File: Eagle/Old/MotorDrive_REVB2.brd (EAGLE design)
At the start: 127 x 58.4 mm, 74 parts, among them J8 J_MC32857, Q1 IRLB3036PBF, Q5 MC7812CTG, Q6 MC7805ACTG, Q7 Q_LTC490, U3 HIP4081A, U4 CD74ACT14, U5 ATMEGA328P, X1 HC49S

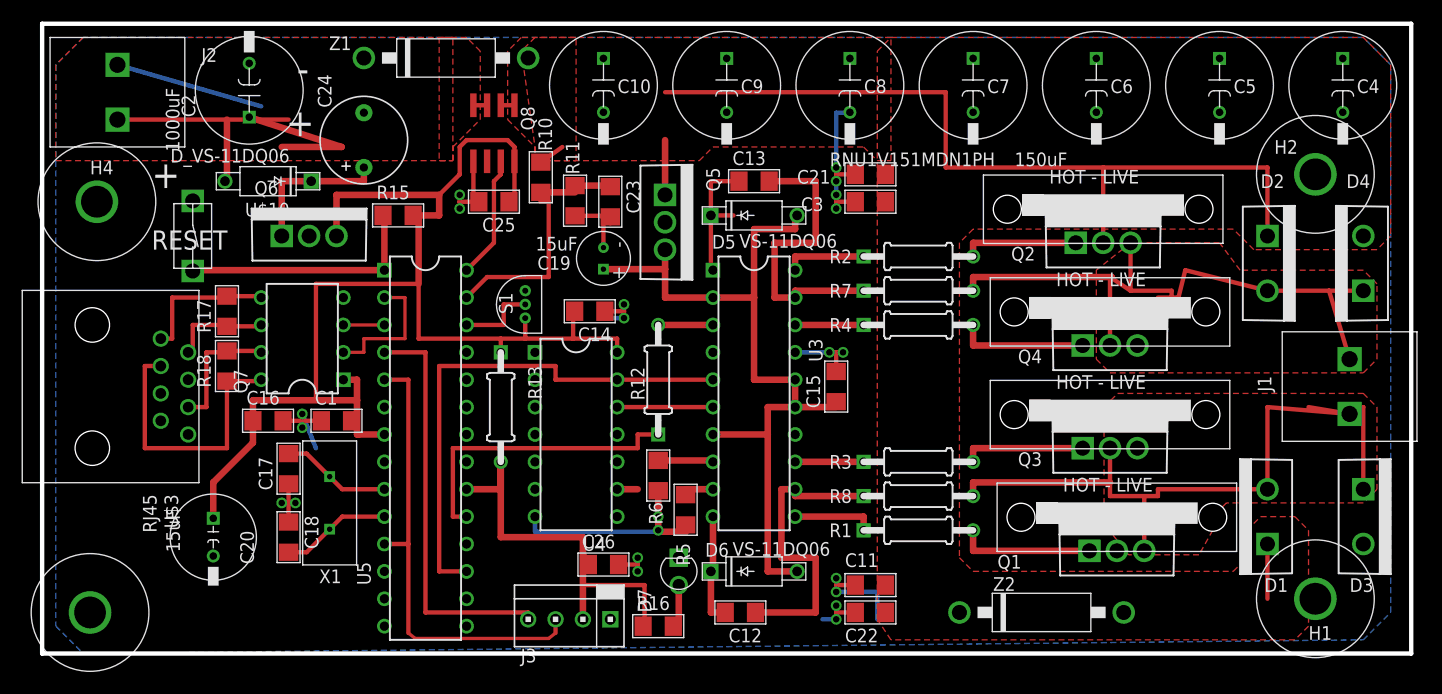
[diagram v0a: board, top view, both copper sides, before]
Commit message: Renamed Revisions, cleaned up PCB silkscreen layer
PCB names for motor drive are now humanly readable.
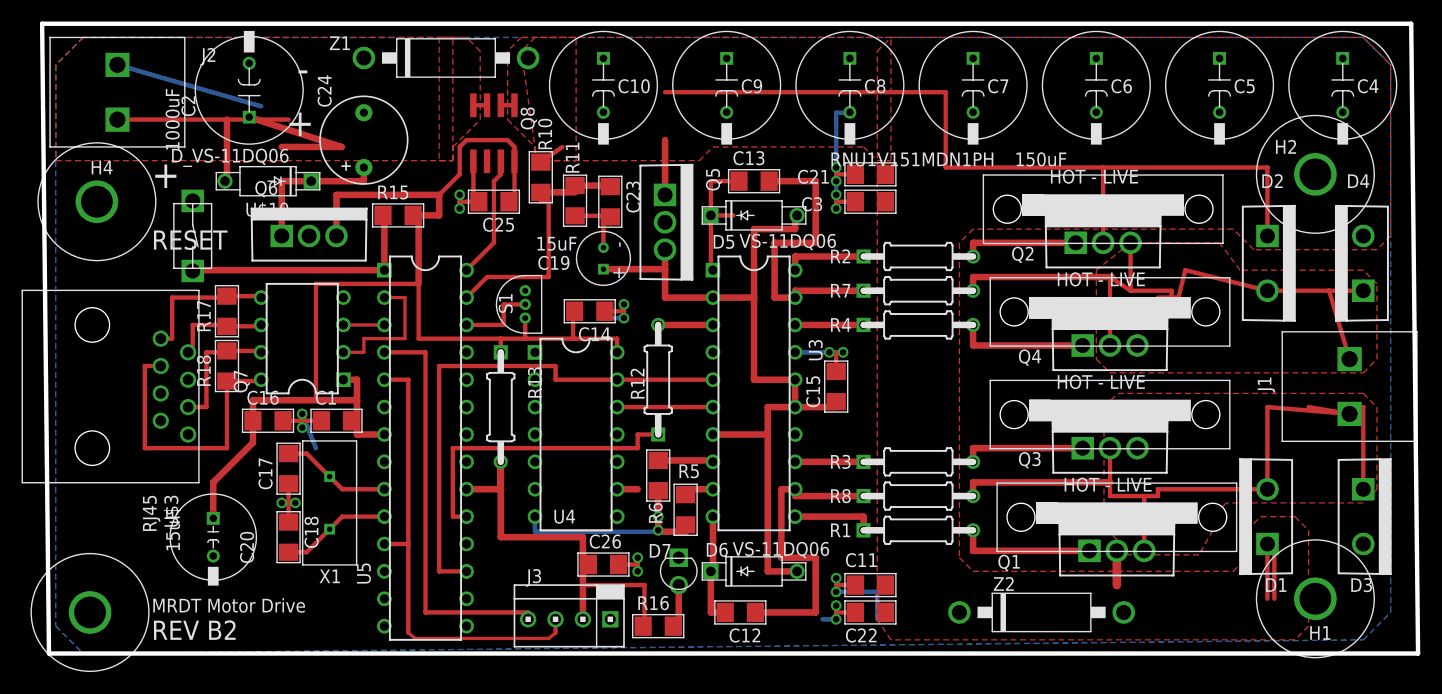
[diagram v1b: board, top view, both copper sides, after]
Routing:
- net V24: track 90.1 -> 99.0 mm
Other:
- board size 127 x 58.4 mm -> 127.6 x 58.4 mm
- board text added: "0.5000 mm / 19.685 mil count= 4"
- board text added: "0.5500 mm / 21.654 mil count= 3"
- board text added: "0.6000 mm / 23.622 mil count= 22"
- board text added: "0.7000 mm / 27.559 mil count= 18"
- board text added: "0.7620 mm / 30.000 mil count= 2"
- board text added: "0.8128 mm / 32.000 mil count= 16"
- board text added: "0.8636 mm / 34.000 mil count= 70"
- board text added: "0.9000 mm / 35.433 mil count= 6"
- board text added: "1.0000 mm / 39.370 mil count= 8"
- board text added: "1.0160 mm / 40.000 mil count= 4"
- board text added: "1.1430 mm / 45.000 mil count= 2"
- board text added: "1.3970 mm / 55.000 mil count= 30"
- board text added: "1.4000 mm / 55.118 mil count= 2"
- board text added: "1.5000 mm / 59.055 mil count= 4"
- board text added: "2.6000 mm / 102.362 mil count= 8"
- board text added: "2.9464 mm / 116.000 mil count= 4"
- board text added: "3.2000 mm / 125.984 mil count= 2"
- board text added: "Date: 1/30/2014 1:14:33 PM"
- board text added: "Drill legend"
- board text added: "MRDT Motor Drive"
- board text added: "Motor Drive RevB2"
- board text added: "REV B2"
- board text removed: "PCBM5 RevA"
